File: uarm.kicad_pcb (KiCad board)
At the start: 2 copper layers, 102.9 x 52.1 mm, 15 parts, among them P1 CONN_01X02, U1 LM2596_Buck_Board, U2 MicroView, U3 esp-01, U4 LM2596_Buck_Board

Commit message: simplified routing
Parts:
- moved U3 23.0 mm to (118.1, 109.2), turned to 180 degrees
- moved P1 19.1 mm to (113.0, 129.5)
- moved R2 14.0 mm to (115.6, 113.0)
- moved CONN4 12.7 mm to (71.1, 114.3)
- moved CONN5 6.35 mm to (71.1, 110.5)
- moved CONN7 6.35 mm to (71.1, 102.9)
- turned C1 to 270 degrees
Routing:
- net GND: track 254.7 -> 0.00 mm
- net ESP_TX: track 49.1 -> 10.7 mm
- net ESP_RST: track 59.4 -> 38.1 mm, vias 0 -> 1
- net MV_RESET: track 39.2 -> 57.9 mm
- net ESP_RX: track 32.1 -> 16.9 mm, vias 0 -> 2
- net MV_RXD: track 37.4 -> 44.3 mm
- net Net-(P1-Pad2): track 26.0 -> 19.2 mm
- net SERVO_HROT: track 34.8 -> 40.1 mm
- net SERVO_H: track 59.1 -> 55.8 mm, vias 0 -> 2
- net SERVO_ROT: track 36.9 -> 39.6 mm, vias 1 -> 0
- net SERVO_L: track 41.1 -> 38.5 mm
- net 3V3: track 65.8 -> 66.5 mm
- net SERVO_R: vias 1 -> 0
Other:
- net class +V: via_dia 0.889 -> 0.95; via_drill 0.635 -> 0.7
- net class Default: via_dia 0.889 -> 0.95; via_drill 0.635 -> 0.7
- net class GND: via_dia 0.889 -> 0.95; via_drill 0.635 -> 0.7
- board text removed: "dacb 2014"

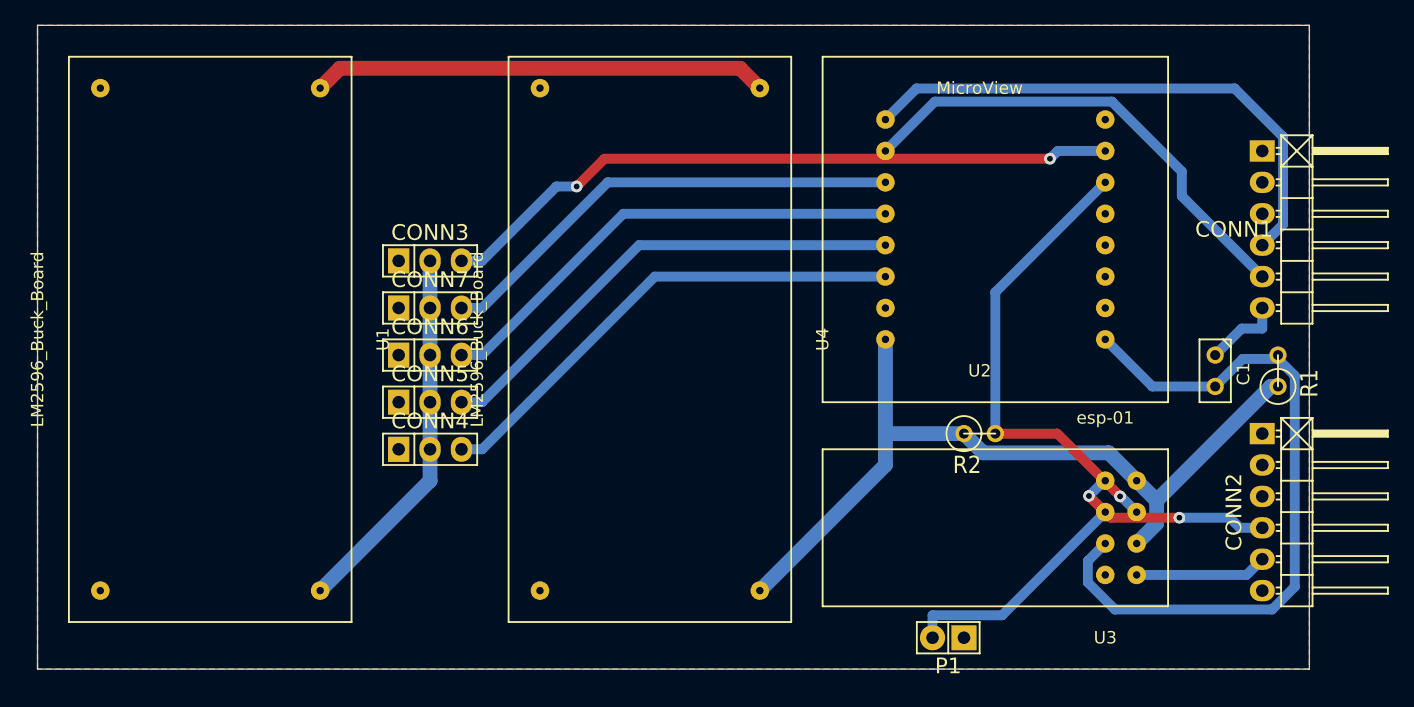
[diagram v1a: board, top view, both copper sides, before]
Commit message: first working prototype created
dropped mutal reset pin handling from esp and microview; now esets
have to occur in software or via a hard power down/up

rotated LM2569 boards to simplify routing

this design has been milled and soldered and works perfectly for
programming both the microview and esp-01 with a FTDI ft232r 3v3
cable.
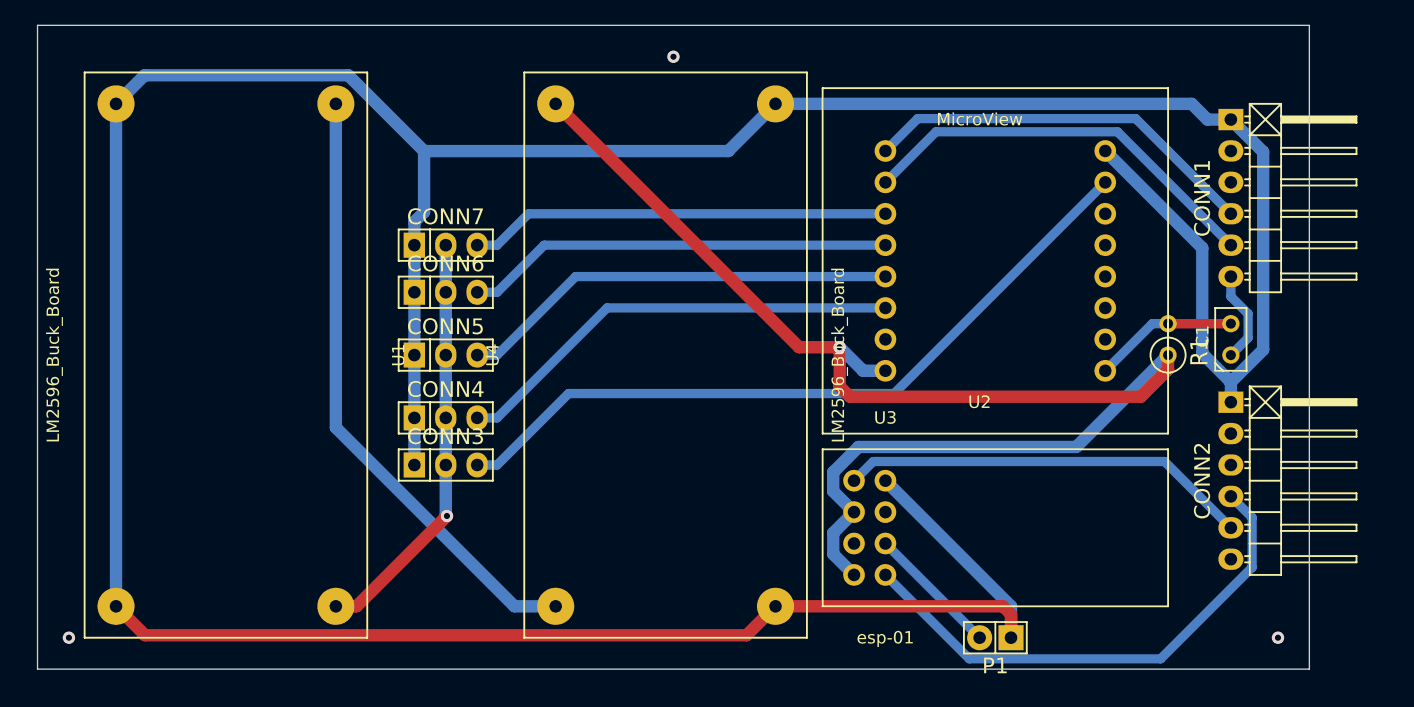
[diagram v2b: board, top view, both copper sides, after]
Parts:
- removed R2: 10K, Discret:R1
- moved U3 23.0 mm to (115.6, 132.1), turned to 0 degrees
- moved CONN3 16.6 mm to (72.4, 115.6)
- moved U4 12.0 mm to (91.4, 111.8), turned to 90 degrees
- moved R1 9.25 mm to (130.8, 105.4)
- moved CONN6 5.24 mm to (72.4, 101.6)
- moved CONN7 5.24 mm to (72.4, 97.8)
- moved CONN5 4.02 mm to (72.4, 106.7)
- moved P1 3.81 mm to (116.8, 129.5)
- moved CONN1 3.59 mm to (135.9, 94.0)
- moved CONN2 3.59 mm to (135.9, 116.8)
- moved C1 2.84 mm to (135.9, 105.4), turned to 90 degrees
- moved CONN4 2.84 mm to (72.4, 111.8)
- moved U2 2.54 mm to (115.6, 97.8)
- moved U1 1.80 mm to (53.3, 101.6)
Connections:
- U2 pad 6: ESP_RST -> Net-(U2-Pad6)
- U3 pad 3: ESP_RST -> Net-(U3-Pad3)
- U3 pad 6: MV_RESET -> Net-(U3-Pad6)
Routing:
- net GND: track 0.00 -> 303.5 mm
- net MV_RESET: track 57.9 -> 11.7 mm
- net 3V3: track 66.5 -> 109.2 mm, vias 0 -> 1
- net ESP_RST: track 38.1 -> 0.00 mm, vias 1 -> 0
- net ESP_RX: track 16.9 -> 42.0 mm, vias 2 -> 0
- net ESP_TX: track 10.7 -> 33.3 mm
- net VCC: track 36.9 -> 50.0 mm
- net MV_RXD: track 44.3 -> 32.2 mm
- net Net-(P1-Pad2): track 19.2 -> 10.8 mm
- net MV_TXD: track 39.2 -> 33.4 mm
- net SERVO_H: track 55.8 -> 60.3 mm, vias 2 -> 0
- net SERVO_R: track 39.0 -> 34.6 mm
- net SERVO_L: track 38.5 -> 34.1 mm
- net SERVO_ROT: track 39.6 -> 35.7 mm
- net +5V: track 30.4 -> 34.0 mm, vias 0 -> 1
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- removed copper zone on B.Cu, net GND
- removed copper zone on F.Cu, net GND
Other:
- net class +V: clearance 0.254 -> 0.3; trace_width 1.2 -> 1; via_dia 0.95 -> 1
- net class Default: clearance 0.254 -> 0.3; trace_width 0.8 -> 0.75; via_dia 0.95 -> 1
- net class GND: clearance 0.254 -> 0.3; trace_width 1.2 -> 1; via_dia 0.95 -> 1
- rule trace_clearance: 0.254 -> 0.3
- rule trace_min: 0.254 -> 0.75
- rule via_min_drill: 0.508 -> 0.7
- rule via_min_size: 0.889 -> 1
